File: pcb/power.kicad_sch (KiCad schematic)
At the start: 31 parts, among them J8 USB_C_Receptacle_USB2.0_14P, P1 Conn_WallPlug_Earth, Q2 Q_PMOS_DGS, Q3 Q_NMOS_DGS, SW1 PWR, SW2 KILL, U4 SRV05-4, U6 ME6118A

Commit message: Further enhancementss
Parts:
- J8: LCSC (none) -> C165948
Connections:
- net +5V: no longer U4.5 (VP)
- net VBUS: now reaches F3.1, J8.A4 (VBUS), J8.A9 (VBUS), J8.B4 (VBUS), J8.B9 (VBUS)
- net VBUS: now also U4.5 (VP)
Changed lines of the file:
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@@
 	)
 	(junction
+		(at 130.81 63.5)
+		(diameter 0)
+		(color 0 0 0 0)
+	)
+	(junction
 		(at 101.6 123.19)
 		(diameter 0)
@@
 	(wire
 		(pts
-			(xy 129.54 63.5) (xy 133.35 63.5)
+			(xy 129.54 63.5) (xy 130.81 63.5)
 		)
 		(stroke
@@
 	(wire
 		(pts
+			(xy 130.81 63.5) (xy 133.35 63.5)
+		)
+		(stroke
+			(width 0)
+			(type default)
+		)
+	)
+	(wire
+		(pts
 			(xy 115.57 91.44) (xy 115.57 95.25)
 		)
@@
 	(wire
 		(pts
+			(xy 208.28 123.19) (xy 217.17 123.19)
+		)
+		(stroke
+			(width 0)
+			(type default)
+		)
+	)
+	(wire
+		(pts
 			(xy 101.6 135.89) (xy 113.03 135.89)
 		)
@@
 		)
 	)
+	(wire
+		(pts
+			(xy 130.81 60.96) (xy 130.81 63.5)
+		)
+		(stroke
+			(width 0)
+			(type default)
+		)
+	)
 	(text "Soft switch"
 		(exclude_from_sim no)
@@
 		)
 	)
+	(label "LA"
+		(at 217.17 123.19 180)
+		(fields_autoplaced yes)
+		(effects
+			(font
+				(size 1.27 1.27)
+			)
+			(justify right bottom)
+		)
+	)
 	(label "D-"
 		(at 137.16 81.28 180)
@@
 		(dnp no)
 		(property "Reference" "R12"
-			(at 135.382 73.66 90)
+			(at 134.874 73.66 90)
 			(effects
 				(font
@@
 		(on_board yes)
 		(dnp no)
-		(fields_autoplaced yes)
 		(property "Reference" "J8"
 			(at 115.57 56.8155 0)
@@
 		)
 		(property "Value" "USB_C_Receptacle_USB2.0_14P"
-			(at 115.57 59.2398 0)
+			(at 109.982 59.182 0)
 			(effects
 				(font
@@
 			)
 		)
-		(property "Datasheet" "https://www.usb.org/sites/default/files/documents/usb_type-c.zip"
+		(property "Datasheet" "https://datasheet.lcsc.com/lcsc/2205251630_Korean-Hroparts-Elec-TYPE-C-31-M-12_C165948.pdf"
 			(at 119.38 78.74 0)
 			(effects
@@
 			)
 		)
+		(property "LCSC" "C165948"
+			(at 115.57 78.74 0)
+			(effects
+				(font
+					(size 1.27 1.27)
+				)
+				(hide yes)
+			)
+		)
 		(pin "B6"
 		)
@@
 	)
 	(symbol
-		(lib_id "power:+5V")
-		(at 78.74 53.34 0)
-		(unit 1)
-		(exclude_from_sim no)
-		(in_bom yes)
-		(on_board yes)
-		(dnp no)
-		(fields_autoplaced yes)
-		(property "Reference" "#PWR074"
-			(at 78.74 57.15 0)
-			(effects
-				(font
-					(size 1.27 1.27)
-				)
-				(hide yes)
-			)
-		)
-		(property "Value" "+5V"
-			(at 78.74 49.2069 0)
-			(effects
-				(font
-					(size 1.27 1.27)
-				)
-			)
-		)
-		(property "Footprint" ""
-			(at 78.74 53.34 0)
-			(effects
-				(font
-					(size 1.27 1.27)
-				)
-				(hide yes)
-			)
-		)
-		(property "Datasheet" ""
-			(at 78.74 53.34 0)
-			(effects
-				(font
-					(size 1.27 1.27)
-				)
-				(hide yes)
-			)
-		)
-		(property "Description" "Power symbol creates a global label with name \"+5V\""
-			(at 78.74 53.34 0)
-			(effects
-				(font
-					(size 1.27 1.27)
-				)
-				(hide yes)
-			)
-		)
-		(pin "1"
-		)
-		(instances
-			(project "board-burner"
-				(path "/8e8c1c81-e974-4404-a855-b409907250d2/984732a5-2bc4-4187-ad41-98eb9e6157f7"
-					(reference "#PWR074")
-					(unit 1)
-				)
-			)
-		)
-	)
-	(symbol
 		(lib_id "Device:R")
 		(at 160.02 144.78 90)
@@
 	)
 	(symbol
+		(lib_id "power:VBUS")
+		(at 130.81 60.96 0)
+		(unit 1)
+		(exclude_from_sim no)
+		(in_bom yes)
+		(on_board yes)
+		(dnp no)
+		(fields_autoplaced yes)
+		(property "Reference" "#PWR042"
+			(at 130.81 64.77 0)
+			(effects
+				(font
+					(size 1.27 1.27)
+				)
+				(hide yes)
+			)
+		)
+		(property "Value" "VBUS"
+			(at 130.81 56.8269 0)
+			(effects
+				(font
+					(size 1.27 1.27)
+				)
+			)
+		)
+		(property "Footprint" ""
+			(at 130.81 60.96 0)
+			(effects
+				(font
+					(size 1.27 1.27)
+				)
+				(hide yes)
+			)
+		)
+		(property "Datasheet" ""
+			(at 130.81 60.96 0)
+			(effects
+				(font
+					(size 1.27 1.27)
+				)
+				(hide yes)
+			)
+		)
+		(property "Description" "Power symbol creates a global label with name \"VBUS\""
+			(at 130.81 60.96 0)
+			(effects
+				(font
+					(size 1.27 1.27)
+				)
+				(hide yes)
+			)
+		)
+		(pin "1"
+		)
+		(instances
+			(project "board-burner"
+				(path "/8e8c1c81-e974-4404-a855-b409907250d2/984732a5-2bc4-4187-ad41-98eb9e6157f7"
+					(reference "#PWR042")
+					(unit 1)
+				)
+			)
+		)
+	)
+	(symbol
 		(lib_id "power:+3V3")
 		(at 213.36 21.59 0)
@@
 		(dnp no)
 		(property "Reference" "R13"
-			(at 135.382 66.294 90)
+			(at 134.874 66.294 90)
 			(effects
 				(font
@@
 					(unit 1)
 				)
+			)
+		)
+	)
+	(symbol
+		(lib_id "power:VBUS")
+		(at 78.74 53.34 0)
+		(unit 1)
+		(exclude_from_sim no)
+		(in_bom yes)
+		(on_board yes)
+		(dnp no)
+		(fields_autoplaced yes)
+		(property "Reference" "#PWR043"
+			(at 78.74 57.15 0)
+			(effects
+				(font
+					(size 1.27 1.27)
+				)
+				(hide yes)
+			)
+		)
+		(property "Value" "VBUS"
+			(at 78.74 49.2069 0)
+			(effects
+				(font
+					(size 1.27 1.27)
+				)
+			)
+		)
+		(property "Footprint" ""
+			(at 78.74 53.34 0)
+			(effects
+				(font
+					(size 1.27 1.27)
+				)
+				(hide yes)
+			)
+		)
+		(property "Datasheet" ""
+			(at 78.74 53.34 0)
+			(effects
+				(font
+					(size 1.27 1.27)
+				)
+				(hide yes)
+			)
+		)
+		(property "Description" "Power symbol creates a global label with name \"VBUS\""
+			(at 78.74 53.34 0)
+			(effects
+				(font
+					(size 1.27 1.27)
+				)
+				(hide yes)
+			)
+		)
+		(pin "1"
+		)
+		(instances
+			(project "board-burner"
+				(path "/8e8c1c81-e974-4404-a855-b409907250d2/984732a5-2bc4-4187-ad41-98eb9e6157f7"
+					(reference "#PWR043")
+					(unit 1)
+				)

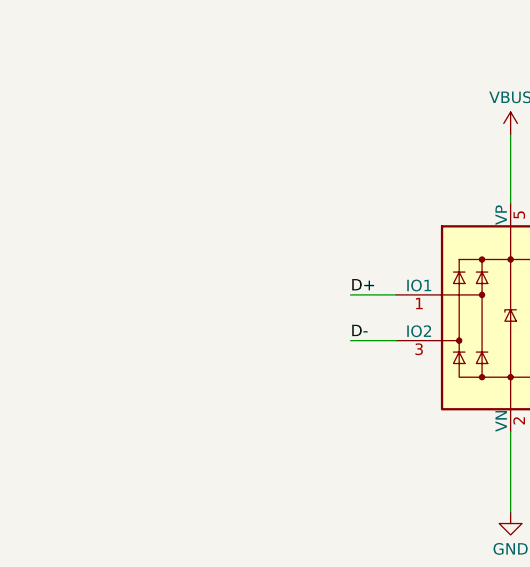
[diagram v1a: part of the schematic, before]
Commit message: Added some transient protection
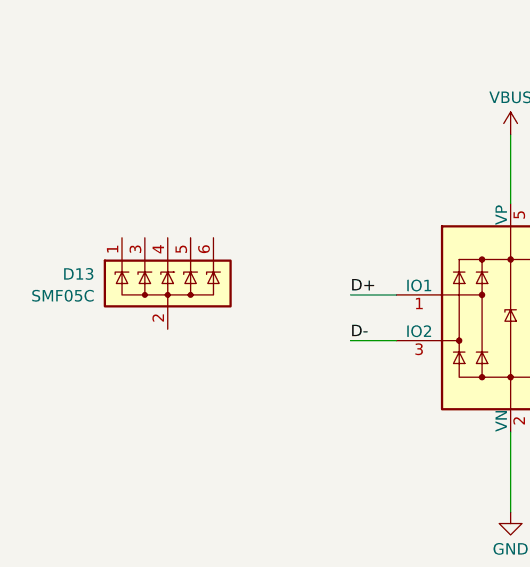
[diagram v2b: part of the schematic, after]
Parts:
- added D13: SMF05C, Package_TO_SOT_SMD:SOT-363_SC-70-6_Handsoldering, symbol Power_Protection:SP0505BAHT
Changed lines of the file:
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@@
+	)
+	(symbol
+		(lib_id "Power_Protection:SP0505BAHT")
+		(at 40.64 69.85 0)
+		(unit 1)
+		(exclude_from_sim no)
+		(in_bom yes)
+		(on_board yes)
+		(dnp no)
+		(property "Reference" "D13"
+			(at 32.512 68.834 0)
+			(effects
+				(font
+					(size 1.27 1.27)
+				)
+				(justify right)
+			)
+		)
+		(property "Value" "SMF05C"
+			(at 32.512 71.2583 0)
+			(effects
+				(font
+					(size 1.27 1.27)
+				)
+				(justify right)
+			)
+		)
+		(property "Footprint" "Package_TO_SOT_SMD:SOT-363_SC-70-6_Handsoldering"
+			(at 48.26 71.12 0)
+			(effects
+				(font
+					(size 1.27 1.27)
+				)
+				(justify left)
+				(hide yes)
+			)
+		)
+		(property "Datasheet" "https://wmsc.lcsc.com/wmsc/upload/file/pdf/v2/lcsc/2108131930_TECH-PUBLIC-SMF05C_C558425.pdf"
+			(at 43.815 66.675 0)
+			(effects
+				(font
+					(size 1.27 1.27)
+				)
+				(hide yes)
+			)
+		)
+		(property "Description" "TVS Diode Array, 5.5V Standoff, 5 Channels, SOT-363 package"
+			(at 40.64 69.85 0)
+			(effects
+				(font
+					(size 1.27 1.27)
+				)
+				(hide yes)
+			)
+		)
+		(property "LCSC" "C558425"
+			(at 40.64 69.85 0)
+			(effects
+				(font
+					(size 1.27 1.27)
+				)
+				(hide yes)
+			)
+		)
+		(pin "3"
+		)
+		(pin "5"
+		)
+		(pin "2"
+		)
+		(pin "1"
+		)
+		(pin "4"
+		)
+		(pin "6"
+		)
+		(instances
+			(project "board-burner"
+				(path "/8e8c1c81-e974-4404-a855-b409907250d2/984732a5-2bc4-4187-ad41-98eb9e6157f7"
+					(reference "D13")
+					(unit 1)
+				)
+			)
+		)
 	)
 	(symbol
